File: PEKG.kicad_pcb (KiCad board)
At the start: 2 copper layers, 56 parts, among them J1 USB_C_Receptacle, J2 Klema, J3 Klema, U1 TL072, U10 74LVC1G125, U11 74LVC1G125, U2 TL072, U3 TL072, U5 TS5A63157DBV, U6 TS5A63157DBV, U7 TS5A63157DBV, U9 74LVC1G125

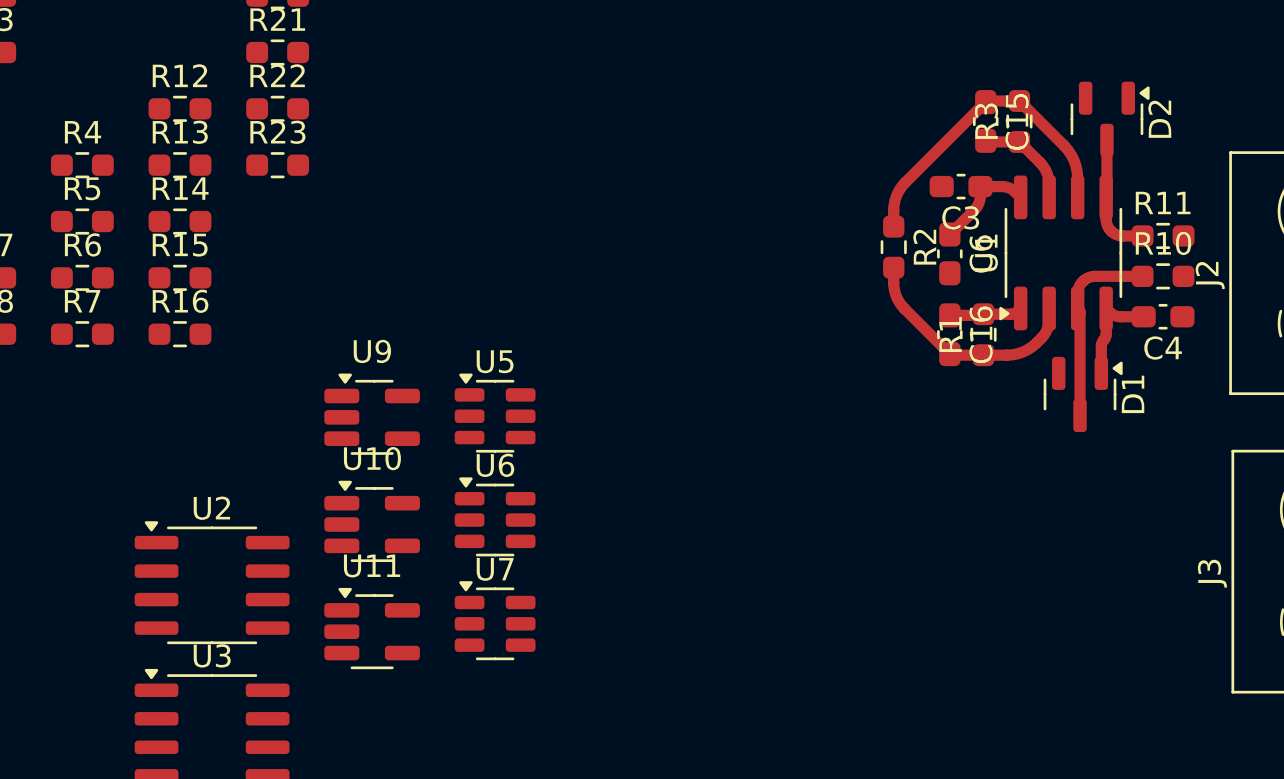
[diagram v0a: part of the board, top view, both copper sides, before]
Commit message: Changed input opamps to NCS.
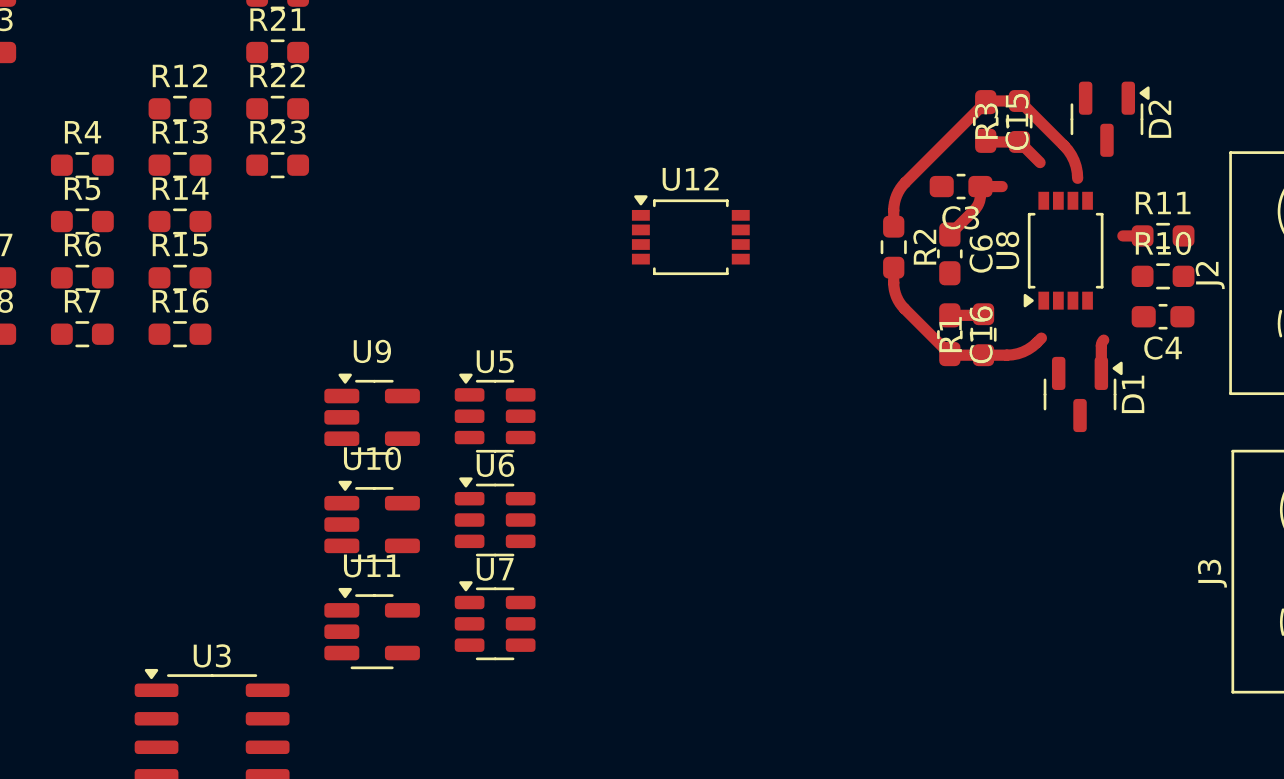
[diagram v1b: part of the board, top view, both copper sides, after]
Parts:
- removed U1, U2: TL072, Package_SO:SOIC-8_3.9x4.9mm_P1.27mm
- added U12: NCS21802DMR2G, Package_SO:OnSemi_Micro8, F.Cu at (181.0, 87.7)
- added U8: NCS21802DMR2G, Package_SO:OnSemi_Micro8, F.Cu at (197.7, 88.3)
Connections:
- J1 pad A5: unconnected-(J1-CC1-PadA5) -> GND
- J1 pad B5: unconnected-(J1-CC2-PadB5) -> GND
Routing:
- net Net-(U8A-+): track 8.78 -> 0.00 mm
- net Net-(U8B-+): track 5.57 -> 0.88 mm
- net VEE: track 4.46 -> 1.51 mm
- net Net-(C16-Pad1): track 3.25 -> 1.55 mm
- net Net-(C15-Pad2): track 4.47 -> 2.82 mm
- net Net-(U8A--): track 10.5 -> 9.13 mm
- net VCC: track 4.43 -> 3.44 mm
- net Net-(U8B--): track 14.0 -> 13.1 mm

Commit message: Little PCB modifications.
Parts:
- removed J3: Klema, TerminalBlock:TerminalBlock_MaiXu_MX126-5.0-02P_1x02_P5.00mm
- removed U3: TL072, Package_SO:SOIC-8_3.9x4.9mm_P1.27mm
- added C21: 10u, Capacitor_SMD:C_0603_1608Metric_Pad1.08x0.95mm_HandSolder, F.Cu at (140.6, 126.6)
- added C22: 10u, Capacitor_SMD:C_0603_1608Metric_Pad1.08x0.95mm_HandSolder, F.Cu at (140.6, 129.1)
- added C23: 10u, Capacitor_SMD:C_0603_1608Metric_Pad1.08x0.95mm_HandSolder, F.Cu at (140.6, 131.6)
- added C24: 10n, Capacitor_SMD:C_0603_1608Metric_Pad1.08x0.95mm_HandSolder, F.Cu at (126.0, 109.7)
- added C25: 10n, Capacitor_SMD:C_0603_1608Metric_Pad1.08x0.95mm_HandSolder, F.Cu at (126.0, 112.2)
- added C26: 100n, Capacitor_SMD:C_0603_1608Metric_Pad1.08x0.95mm_HandSolder, F.Cu at (126.0, 114.7)
- added C27: 1u, Capacitor_SMD:C_0603_1608Metric_Pad1.08x0.95mm_HandSolder, F.Cu at (126.0, 117.2)
- added G***: LOGO, logo:logo, B.Cu at (115.3, 109.8)
- added H1: MountingHole, MountingHole:MountingHole_3.2mm_M3_ISO14580_Pad_TopBottom, F.Cu at (105.0, 105.0)
- added H2: MountingHole, MountingHole:MountingHole_3.2mm_M3_ISO14580_Pad_TopBottom, F.Cu at (105.0, 140.0)
- added H3: MountingHole, MountingHole:MountingHole_3.2mm_M3_ISO14580_Pad_TopBottom, F.Cu at (185.0, 105.0)
- added H4: MountingHole, MountingHole:MountingHole_3.2mm_M3_ISO14580_Pad_TopBottom, F.Cu at (185.0, 140.0)
- added R17: 100k, Resistor_SMD:R_0603_1608Metric_Pad0.98x0.95mm_HandSolder, F.Cu at (144.9, 129.1)
- added R24: 100k, Resistor_SMD:R_0603_1608Metric_Pad0.98x0.95mm_HandSolder, F.Cu at (144.9, 136.6)
- added R25: 190k, Resistor_SMD:R_0603_1608Metric_Pad0.98x0.95mm_HandSolder, F.Cu at (130.3, 114.7)
- added R26: 10k, Resistor_SMD:R_0603_1608Metric_Pad0.98x0.95mm_HandSolder, F.Cu at (130.3, 117.2)
- added R27: 10k, Resistor_SMD:R_0603_1608Metric_Pad0.98x0.95mm_HandSolder, F.Cu at (138.0, 106.5)
- added R28: 20k, Resistor_SMD:R_0603_1608Metric_Pad0.98x0.95mm_HandSolder, F.Cu at (138.0, 109.0)
- added R29: 20k, Resistor_SMD:R_0603_1608Metric_Pad0.98x0.95mm_HandSolder, F.Cu at (138.0, 111.5)
- added R30: 10k, Resistor_SMD:R_0603_1608Metric_Pad0.98x0.95mm_HandSolder, F.Cu at (138.0, 114.0)
- added R31: 10k, Resistor_SMD:R_0603_1608Metric_Pad0.98x0.95mm_HandSolder, F.Cu at (138.0, 116.5)
- added REF**: ele_petnica_logo, PEP_library:ele_petnica_logo, F.Cu at (115.3, 109.8)
- added U13: NCS21802DMR2G, Package_SO:OnSemi_Micro8, F.Cu at (151.9, 130.4)
- added U14: NCS21802DMR2G, Package_SO:OnSemi_Micro8, F.Cu at (132.3, 110.1)
- C7: value 10u -> 100n
- J2: value Klema -> AudioJack3; footprint TerminalBlock:TerminalBlock_MaiXu_MX126-5.0-02P_1x02_P5.00mm -> PEKG:Jack_3.5mm_CUI_SJ1-3523N_Horizontal
- R1, R3: value 1k -> 20k
- R15, R16, R18, R23: value 1k -> 100k
- R2: value 1k -> 10k
- moved C12 70.0 mm to (110.8, 135.3)
- moved C11 70.0 mm to (110.8, 132.8)
- moved C13 70.0 mm to (110.8, 137.8)
- moved C19 70.0 mm to (115.2, 130.3)
- moved C20 70.0 mm to (115.2, 132.8)
- moved R18 62.2 mm to (144.9, 131.6)
- moved R19 61.9 mm to (136.3, 130.5)
- moved R20 61.9 mm to (136.3, 133.0)
- moved R22 61.9 mm to (136.3, 138.0)
- moved R21 61.9 mm to (136.3, 135.5)
- moved C18 58.1 mm to (116.0, 139.4)
- moved R4 58.1 mm to (120.3, 131.9)
- moved R7 58.1 mm to (120.3, 139.4)
- moved R5 58.1 mm to (120.3, 134.4)
- moved C17 58.1 mm to (116.0, 136.9)
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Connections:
- C15 pad 2: Net-(C15-Pad2) -> /BOTTOM
- C16 pad 1: Net-(C16-Pad1) -> /TOP
- C7 pad 1: /DC_COMPENSATION -> VCC
- C7 pad 2: Net-(U3A--) -> GND
- R1 pad 2: Net-(C16-Pad1) -> /TOP
- R10 pad 2: POSITIVE_INPUT -> LEFT_ARM
- R11 pad 2: NEGATIVE_INPUT -> RIGHT_ARM
- R14 pad 1: Net-(U3A--) -> Net-(U13A--)
- R14 pad 2: BUFFERS_OUTPUT -> /BOTTOM
- R15 pad 1: Net-(U3B-+) -> Net-(U13A-+)
- R15 pad 2: BUFFERS_OUTPUT -> /TOP
- R16 pad 1: Net-(U3B-+) -> DC_COMPENSATION
- R16 pad 2: /DC_COMPENSATION -> Net-(U13A--)
- R18 pad 1: Net-(U3B--) -> Net-(U13B-+)
- R18 pad 2: OUTPUT -> VCC
- R23 pad 1: GND -> 2.5V
- R23 pad 2: Net-(U3B--) -> Net-(U13B--)
- R3 pad 1: Net-(C15-Pad2) -> /BOTTOM
- R4 pad 2: Net-(C16-Pad1) -> /TOP
- R5 pad 1: Net-(C15-Pad2) -> /BOTTOM
- R6 pad 2: Net-(C16-Pad1) -> /TOP
- R7 pad 2: Net-(C15-Pad2) -> /BOTTOM
- R8 pad 1: BUFFERS_OUTPUT -> GAIN_5_OUTPUT
- R9 pad 1: COMMON_OUTPUT_LEVEL -> DC_COMPENSATION
- U12 pad 1: BUFFERS_OUTPUT -> GAIN_5_OUTPUT
- U8 pad 1: Net-(C16-Pad1) -> /TOP
- U8 pad 7: Net-(C15-Pad2) -> /BOTTOM
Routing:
- net Net-(C15-Pad2): track 2.82 -> 0.00 mm
- net /BOTTOM: track 0.00 -> 2.82 mm
- net Net-(C16-Pad1): track 1.55 -> 0.00 mm
- net /TOP: track 0.00 -> 1.55 mm
- net (no net): vias 0 -> 171
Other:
- board outline added: 90 x 45 mm
- board text added: "PEKG"

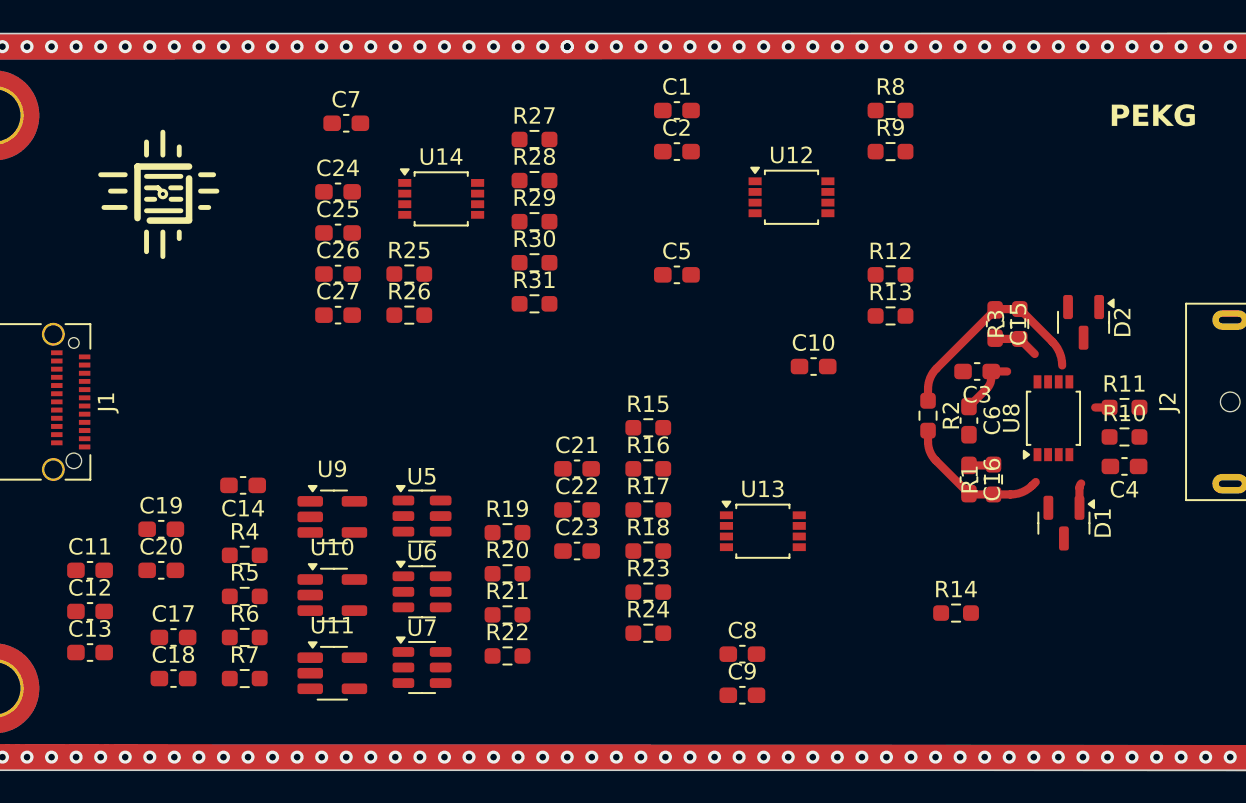
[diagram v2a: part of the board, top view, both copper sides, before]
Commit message: Updates schematic, tests.
Fixed git issue
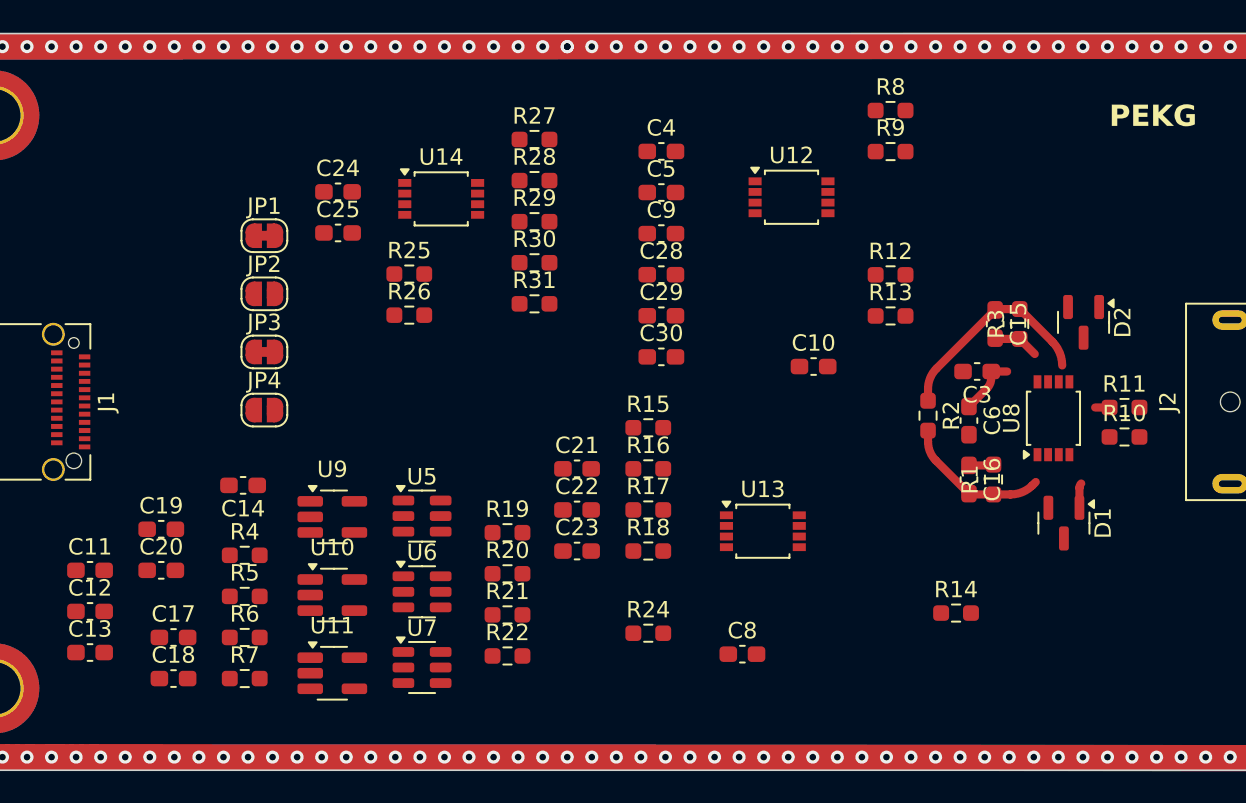
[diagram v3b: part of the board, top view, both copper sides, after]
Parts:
- removed C1, C2, C26, C7: 100n, Capacitor_SMD:C_0603_1608Metric_Pad1.08x0.95mm_HandSolder
- removed C27: 1u, Capacitor_SMD:C_0603_1608Metric_Pad1.08x0.95mm_HandSolder
- removed R23: 100k, Resistor_SMD:R_0603_1608Metric_Pad0.98x0.95mm_HandSolder
- removed REF**: ele_petnica_logo, PEP_library:ele_petnica_logo
- added C28: 10n, Capacitor_SMD:C_0603_1608Metric_Pad1.08x0.95mm_HandSolder, F.Cu at (145.8, 114.7)
- added C29: 10n, Capacitor_SMD:C_0603_1608Metric_Pad1.08x0.95mm_HandSolder, F.Cu at (145.8, 117.2)
- added C30: 1u, Capacitor_SMD:C_0603_1608Metric_Pad1.08x0.95mm_HandSolder, F.Cu at (145.8, 119.8)
- added JP1: Jumper_2_Bridged, Jumper:SolderJumper-2_P1.3mm_Bridged_RoundedPad1.0x1.5mm, F.Cu at (121.5, 112.3)
- added JP2: Jumper_2_Open, Jumper:SolderJumper-2_P1.3mm_Open_RoundedPad1.0x1.5mm, F.Cu at (121.5, 115.9)
- added JP3: Jumper_2_Bridged, Jumper:SolderJumper-2_P1.3mm_Bridged_RoundedPad1.0x1.5mm, F.Cu at (121.5, 119.5)
- added JP4: Jumper_2_Open, Jumper:SolderJumper-2_P1.3mm_Open_RoundedPad1.0x1.5mm, F.Cu at (121.5, 123.0)
- C5: value 1u -> 100n
- C9: value 100n -> 1u
- R13: value 100 -> 1
- R25: value 190k -> 100k
- R8, R9: value 1k -> 100k
- moved C4 34.2 mm to (145.8, 107.2), turned to 0 degrees
- moved C9 28.6 mm to (145.8, 112.2)
- moved C5 5.12 mm to (145.8, 109.7)
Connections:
- net GAIN_5_OUTPUT renamed GAIN_500_OUTPUT
- C10 pad 1: VCC -> VBUS
- C10 pad 2: VEE -> GND
- C22 pad 1: DC_COMPENSATION -> Net-(JP2-A)
- C23 pad 1: 2.5V -> Net-(U13B-+)
- C23 pad 2: Net-(U13B--) -> GND
- C24 pad 1: GAIN_100_OUTPUT -> Net-(JP4-A)
- C3 pad 1: VCC -> VBUS
- C4 pad 1: GND -> VBUS
- C4 pad 2: VEE -> GND
- C5 pad 1: VCC -> VBUS
- C5 pad 2: VEE -> GND
- C6 pad 1: VCC -> VBUS
- C6 pad 2: VEE -> GND
- C8 pad 1: VCC -> VBUS
- C9 pad 1: GND -> VBUS
- C9 pad 2: VEE -> GND
- D1 pad 1: VEE -> GND
- D1 pad 2: VCC -> VBUS
- D2 pad 1: VEE -> GND
- D2 pad 2: VCC -> VBUS
- R16 pad 1: DC_COMPENSATION -> Net-(JP2-A)
- R18 pad 2: VCC -> VBUS
- R25 pad 1: GAIN_100_OUTPUT -> Net-(JP4-A)
- R28 pad 2: VCC -> VBUS
- R30 pad 2: GAIN_100_OUTPUT -> GAIN_5000_OUTPUT
- U12 pad 4: VEE -> GND
- U12 pad 5: GND -> 2.5V
- U12 pad 8: VCC -> VBUS
- U13 pad 1: DC_COMPENSATION -> Net-(JP2-A)
- U13 pad 4: VEE -> GND
- U13 pad 6: Net-(U13B--) -> 2.5V
- U13 pad 8: VCC -> VBUS
- U14 pad 1: GAIN_100_OUTPUT -> Net-(JP4-A)
- U14 pad 4: VEE -> GND
- U14 pad 8: VCC -> VBUS
- U8 pad 4: VEE -> GND
- U8 pad 8: VCC -> VBUS
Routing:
- net VCC: track 3.44 -> 0.00 mm
- net VBUS: track 0.00 -> 3.44 mm
- net VEE: track 1.51 -> 0.00 mm
- net GND: track 0.00 -> 1.51 mm
